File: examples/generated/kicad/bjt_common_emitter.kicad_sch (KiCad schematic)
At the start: 11 parts, among them Q1 2N3904

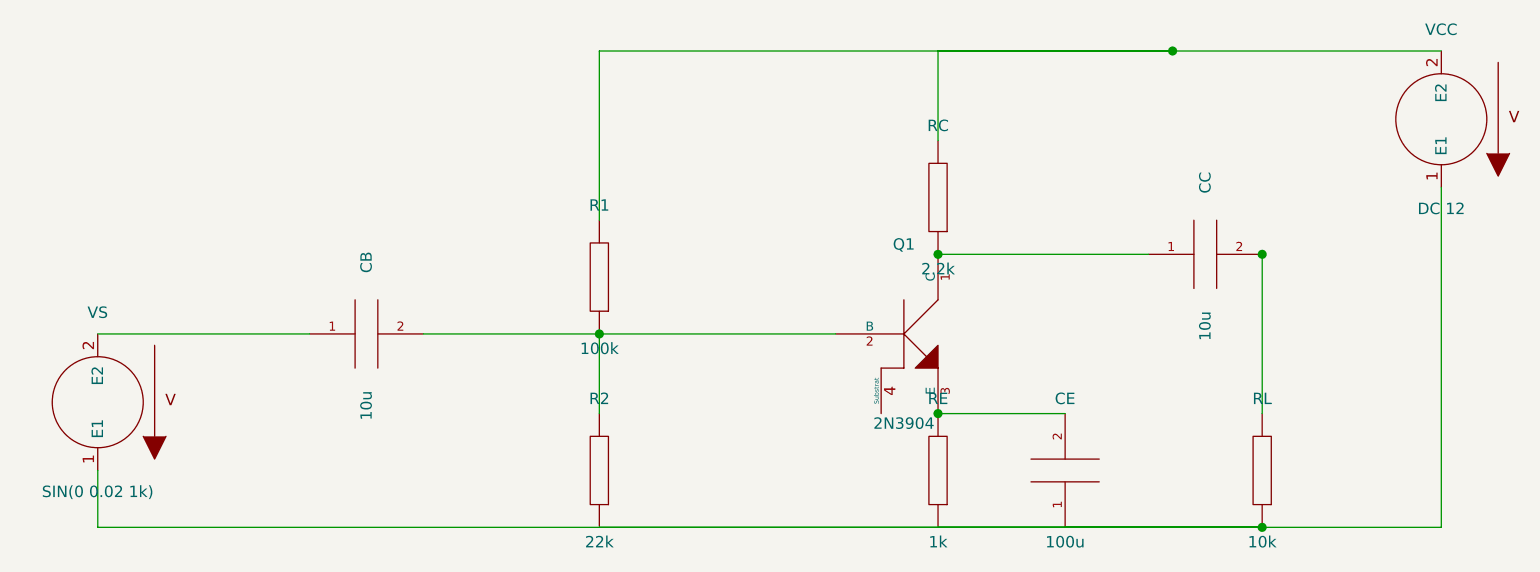
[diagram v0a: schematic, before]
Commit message: Ensure connectivity matches, as measured by opamp connectivity.
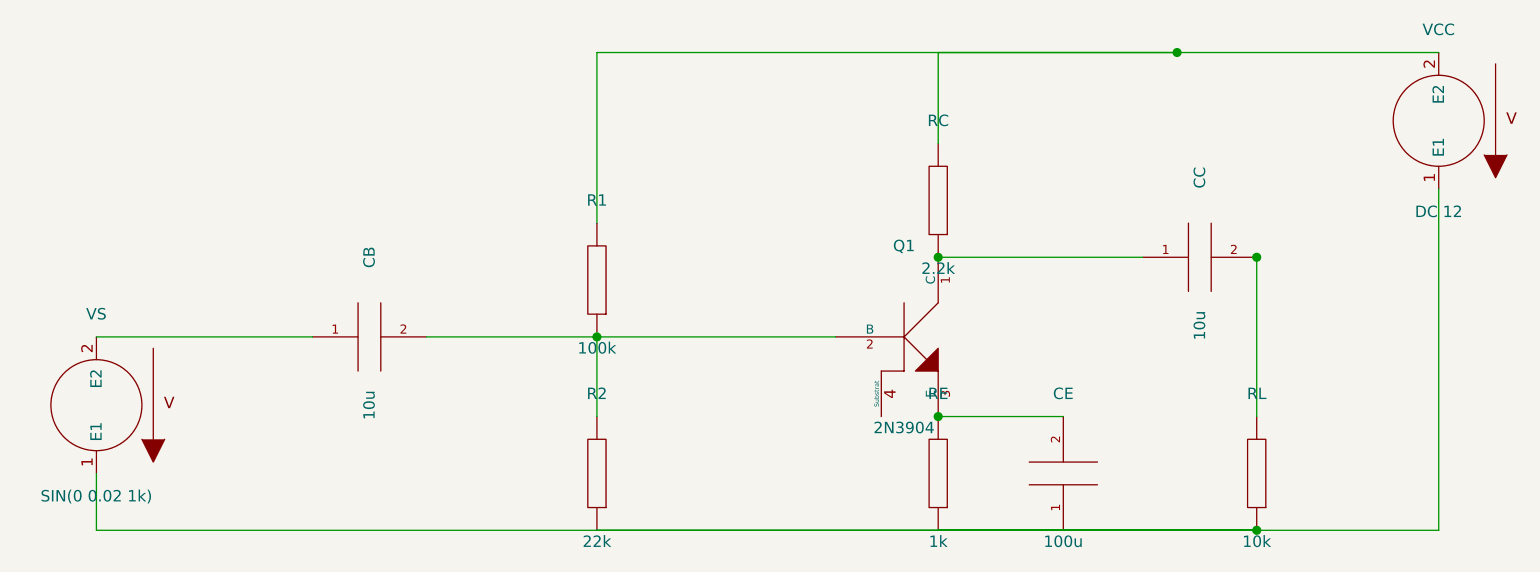
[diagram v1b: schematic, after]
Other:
- moved on the sheet: CC, RL

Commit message: Refactor further.
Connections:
- net vout: now reaches CC.2, RL.2
- net vin_src: now reaches CB.1, VS.2 (E2)
- net emitter: now reaches CE.2, Q1.3 (E), RE.2
- net collector: now reaches CC.1, Q1.1 (C), RC.1
- net base: now reaches CB.2, Q1.2 (B), R1.1, R2.2
- net vcc: now reaches R1.2, RC.2, VCC.2 (E2)
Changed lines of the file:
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@@
     )
+  )
+  (label "vcc" (at 190.50 68.58 0)
+    (effects (font (size 1.27 1.27)))
+  )
+  (label "base" (at 125.73 100.33 0)
+    (effects (font (size 1.27 1.27)))
+  )
+  (label "vin_src" (at 81.28 100.33 0)
+    (effects (font (size 1.27 1.27)))
+  )
+  (label "collector" (at 163.83 91.44 0)
+    (effects (font (size 1.27 1.27)))
+  )
+  (label "emitter" (at 163.83 109.22 0)
+    (effects (font (size 1.27 1.27)))
+  )
+  (label "vout" (at 199.39 91.44 0)
+    (effects (font (size 1.27 1.27)))
   )
   (wire (pts (xy 219.71 68.58) (xy 190.50 68.58))

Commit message: Attempt substrate grounding.
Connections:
- net at CE.1, R2.1, RE.1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: now also Q1.4 (Substrat)
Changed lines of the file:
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@@
   (title_block
     (title "bjt_common_emitter")
-    (date "2026-03-07")
+    (date "2026-03-13")
     (comment 1 "Generated by mixedsig2cad")
   )
@@
     (stroke (width 0) (type solid) (color 0 0 0 0))
   )
-  (wire (pts (xy 69.85 121.92) (xy 199.39 121.92))
-    (stroke (width 0) (type solid) (color 0 0 0 0))
-  )
-  (wire (pts (xy 125.73 121.92) (xy 199.39 121.92))
-    (stroke (width 0) (type solid) (color 0 0 0 0))
-  )
-  (wire (pts (xy 163.83 121.92) (xy 199.39 121.92))
-    (stroke (width 0) (type solid) (color 0 0 0 0))
-  )
-  (wire (pts (xy 177.80 121.92) (xy 199.39 121.92))
+  (wire (pts (xy 69.85 121.92) (xy 157.48 121.92))
+    (stroke (width 0) (type solid) (color 0 0 0 0))
+  )
+  (wire (pts (xy 125.73 121.92) (xy 157.48 121.92))
+    (stroke (width 0) (type solid) (color 0 0 0 0))
+  )
+  (wire (pts (xy 163.83 121.92) (xy 157.48 121.92))
+    (stroke (width 0) (type solid) (color 0 0 0 0))
+  )
+  (wire (pts (xy 177.80 121.92) (xy 157.48 121.92))
+    (stroke (width 0) (type solid) (color 0 0 0 0))
+  )
+  (wire (pts (xy 199.39 121.92) (xy 157.48 121.92))
     (stroke (width 0) (type solid) (color 0 0 0 0))
   )
@@
     (stroke (width 0) (type solid) (color 0 0 0 0))
   )
-  (wire (pts (xy 219.71 121.92) (xy 199.39 121.92))
+  (wire (pts (xy 219.71 121.92) (xy 157.48 121.92))
+    (stroke (width 0) (type solid) (color 0 0 0 0))
+  )
+  (wire (pts (xy 157.48 109.22) (xy 157.48 121.92))
     (stroke (width 0) (type solid) (color 0 0 0 0))
   )
@@
   )
   (junction (at 190.50 68.58) (diameter 1.016) (color 0 0 0 0))
-  (junction (at 199.39 121.92) (diameter 1.016) (color 0 0 0 0))
+  (junction (at 157.48 121.92) (diameter 1.016) (color 0 0 0 0))
   (junction (at 125.73 100.33) (diameter 1.016) (color 0 0 0 0))
   (junction (at 163.83 91.44) (diameter 1.016) (color 0 0 0 0))

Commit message: Attempt to fix routing issues.
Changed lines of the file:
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@@
     (stroke (width 0) (type solid) (color 0 0 0 0))
   )
-  (wire (pts (xy 199.39 109.22) (xy 199.39 91.44))
+  (wire (pts (xy 199.39 91.44) (xy 199.39 109.22))
     (stroke (width 0) (type solid) (color 0 0 0 0))
   )

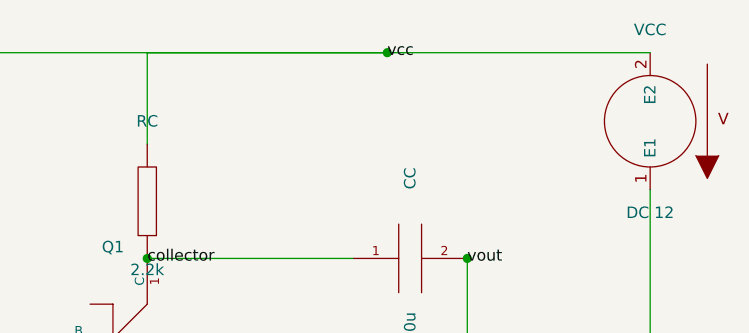
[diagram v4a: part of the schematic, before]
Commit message: Attempt to add the right connections for the schmitt trigger. Messed up cmos inverter.
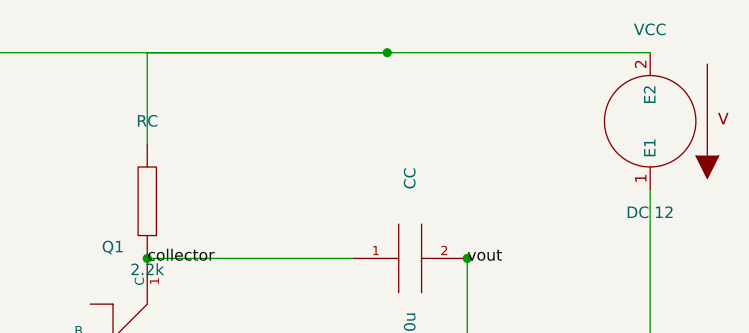
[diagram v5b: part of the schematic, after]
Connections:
- net vcc: no longer names the net of R1.2, RC.2, VCC.2 (E2)
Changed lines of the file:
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@@
   (title_block
     (title "bjt_common_emitter")
-    (date "2026-03-13")
+    (date "2026-03-14")
     (comment 1 "Generated by mixedsig2cad")
   )
@@
     )
   )
-  (label "vcc" (at 190.50 68.58 0)
-    (effects (font (size 1.27 1.27)))
-  )
   (label "base" (at 125.73 100.33 0)

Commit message: Fix CMOS inverter issue.
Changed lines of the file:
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@@
     (stroke (width 0) (type solid) (color 0 0 0 0))
   )
-  (wire (pts (xy 69.85 100.33) (xy 93.98 100.33))
+  (wire (pts (xy 69.85 100.33) (xy 81.28 100.33))
     (stroke (width 0) (type solid) (color 0 0 0 0))
   )
+  (wire (pts (xy 93.98 100.33) (xy 81.28 100.33))
+    (stroke (width 0) (type solid) (color 0 0 0 0))
+  )

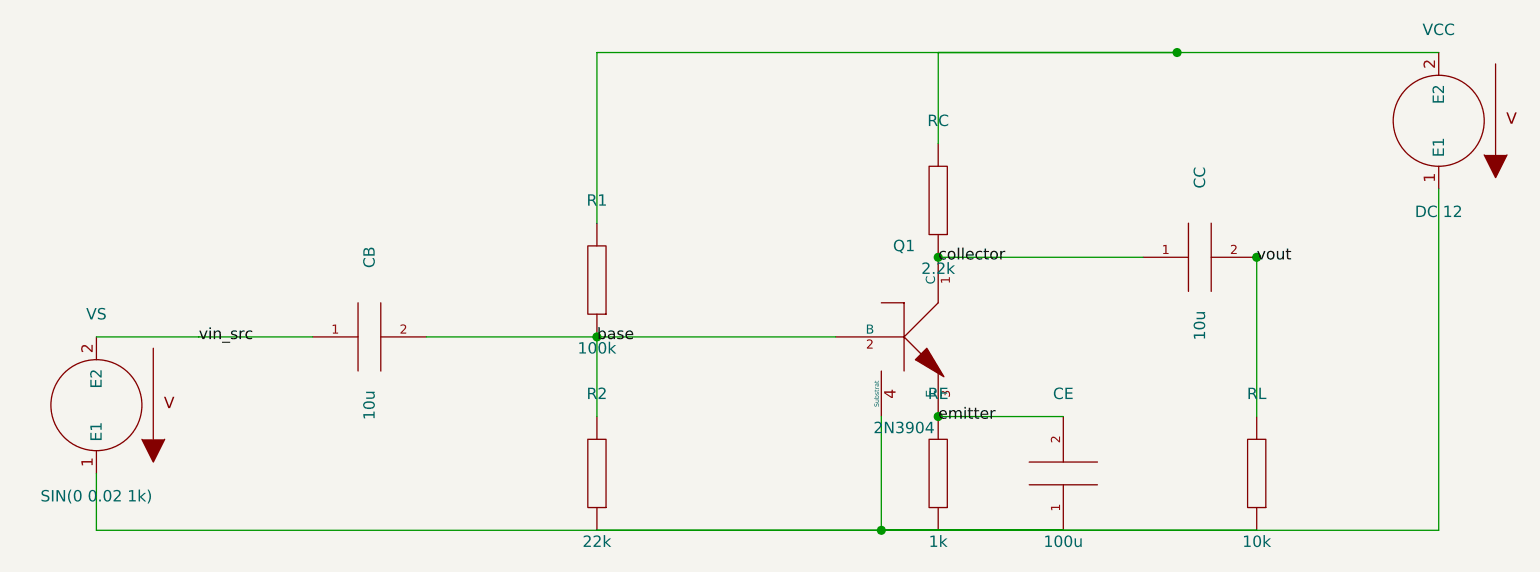
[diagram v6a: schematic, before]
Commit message: Manually change schematics to match what I want.
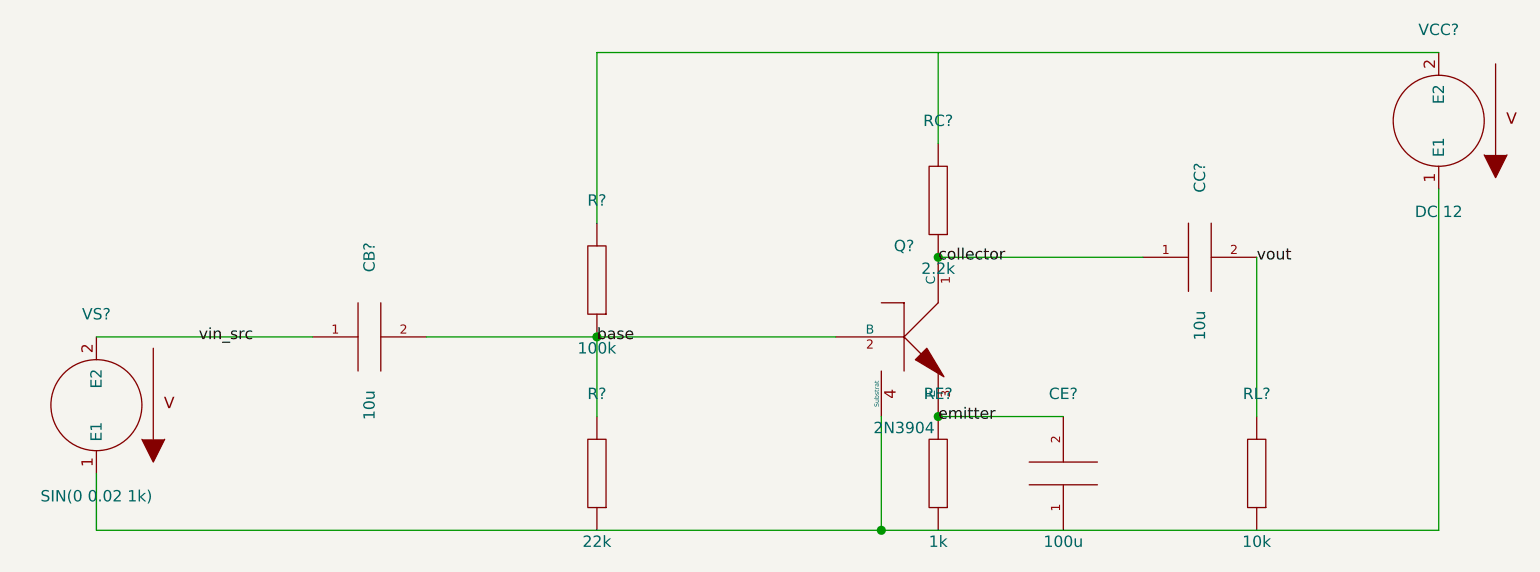
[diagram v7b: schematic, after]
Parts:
- renumbered CB to CB?, CC to CC?, CE to CE?, Q1 to Q?, R1 to R?, R2 to R?, RC to RC?, RE to RE?, RL to RL?, VCC to VCC?, VS to VS?
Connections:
- net at R?.2, VCC?.2 (E2): no longer RC?.2
- new net: Q?.4 (Substrat), VCC?.1 (E1), VS?.1 (E1)
- now unconnected: CE?.1, R?.1, RE?.1, RL?.1

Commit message: Attempt to match manual schematics with seeded layout and generation.
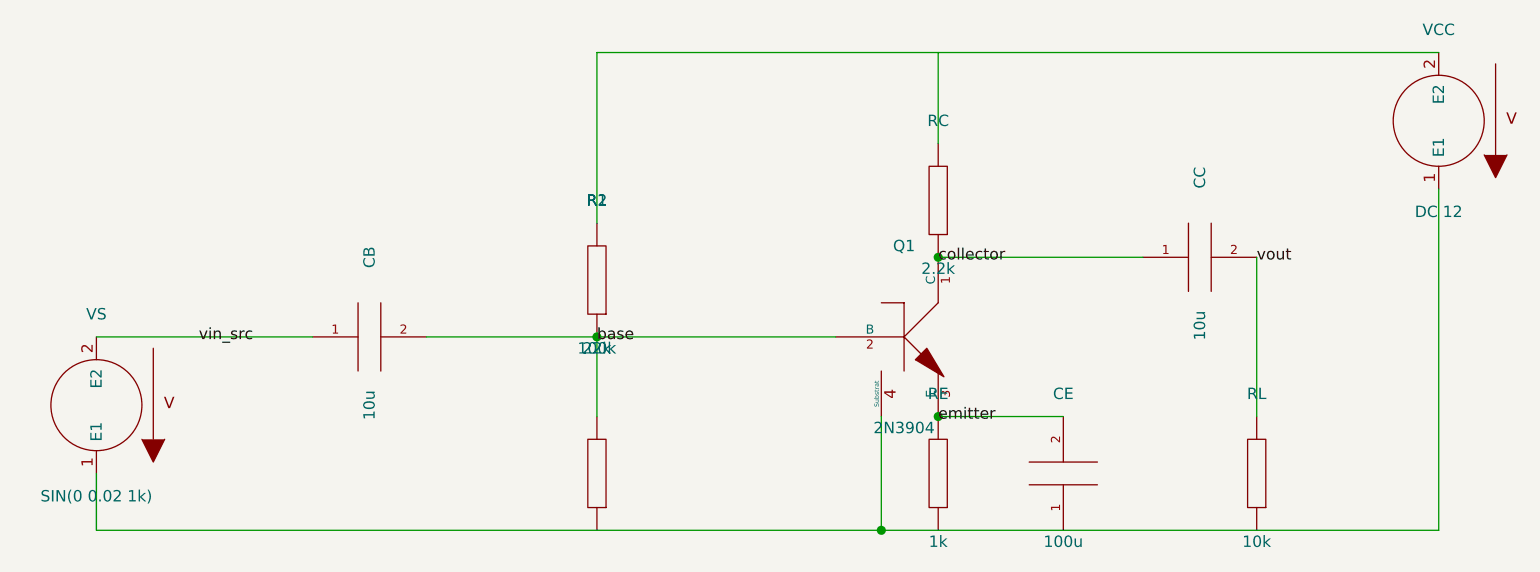
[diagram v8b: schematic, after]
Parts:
- gave numbers to parts that had none: 11
